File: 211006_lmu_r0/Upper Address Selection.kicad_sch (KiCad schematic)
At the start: 8 parts

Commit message: Updated some components to make sourcing easier
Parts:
- R103, R104, R105, R106, R107, R108, R109, R110: Manufacturer (none) -> -; Part Number (none) -> -
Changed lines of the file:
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@@
+      (effects (font (size 1.27 1.27)) hide)
+    )
+    (property "Part Number" "-" (id 4) (at 135.89 92.71 0)
+      (effects (font (size 1.27 1.27)) hide)
+    )
+    (property "Manufacturer" "-" (id 5) (at 135.89 92.71 0)
       (effects (font (size 1.27 1.27)) hide)
     )
@@
       (effects (font (size 1.27 1.27)) hide)
     )
+    (property "Part Number" "-" (id 4) (at 135.89 100.33 0)
+      (effects (font (size 1.27 1.27)) hide)
+    )
+    (property "Manufacturer" "-" (id 5) (at 135.89 100.33 0)
+      (effects (font (size 1.27 1.27)) hide)
+    )
     (pin "1")
     (pin "2")
@@
     )
     (property "Datasheet" "~" (id 3) (at 127 92.71 0)
+      (effects (font (size 1.27 1.27)) hide)
+    )
+    (property "Part Number" "-" (id 4) (at 127 92.71 0)
+      (effects (font (size 1.27 1.27)) hide)
+    )
+    (property "Manufacturer" "-" (id 5) (at 127 92.71 0)
       (effects (font (size 1.27 1.27)) hide)
     )
@@
       (effects (font (size 1.27 1.27)) hide)
     )
+    (property "Part Number" "-" (id 4) (at 127 100.33 0)
+      (effects (font (size 1.27 1.27)) hide)
+    )
+    (property "Manufacturer" "-" (id 5) (at 127 100.33 0)
+      (effects (font (size 1.27 1.27)) hide)
+    )
     (pin "1")
     (pin "2")
@@
     )
     (property "Datasheet" "~" (id 3) (at 143.51 92.71 0)
+      (effects (font (size 1.27 1.27)) hide)
+    )
+    (property "Part Number" "-" (id 4) (at 143.51 92.71 0)
+      (effects (font (size 1.27 1.27)) hide)
+    )
+    (property "Manufacturer" "-" (id 5) (at 143.51 92.71 0)
       (effects (font (size 1.27 1.27)) hide)
     )
@@
       (effects (font (size 1.27 1.27)) hide)
     )
+    (property "Part Number" "-" (id 4) (at 143.51 100.33 0)
+      (effects (font (size 1.27 1.27)) hide)
+    )
+    (property "Manufacturer" "-" (id 5) (at 143.51 100.33 0)
+      (effects (font (size 1.27 1.27)) hide)
+    )
     (pin "1")
     (pin "2")
@@
     )
     (property "Datasheet" "~" (id 3) (at 151.13 92.71 0)
+      (effects (font (size 1.27 1.27)) hide)
+    )
+    (property "Part Number" "-" (id 4) (at 151.13 92.71 0)
+      (effects (font (size 1.27 1.27)) hide)
+    )
+    (property "Manufacturer" "-" (id 5) (at 151.13 92.71 0)
       (effects (font (size 1.27 1.27)) hide)
     )
@@
       (effects (font (size 1.27 1.27)) hide)
     )
+    (property "Part Number" "-" (id 4) (at 151.13 100.33 0)
+      (effects (font (size 1.27 1.27)) hide)
+    )
+    (property "Manufacturer" "-" (id 5) (at 151.13 100.33 0)
+      (effects (font (size 1.27 1.27)) hide)
+    )

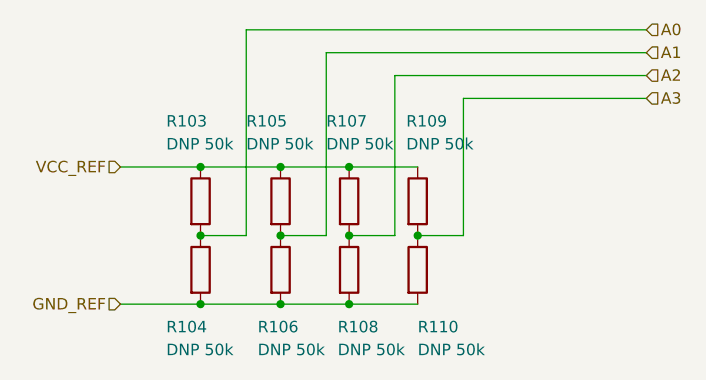
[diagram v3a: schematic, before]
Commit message: Lots of routing and placing, according to planned layout
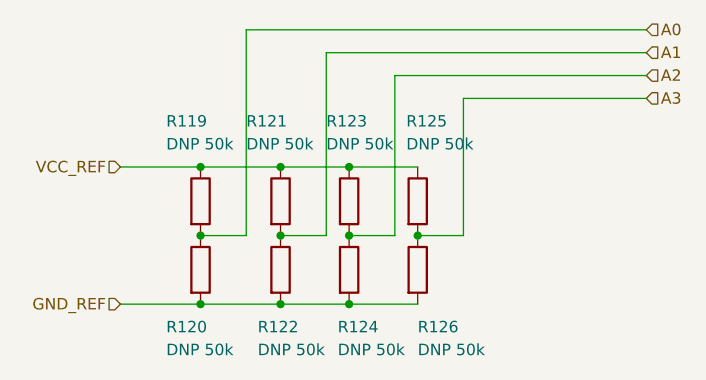
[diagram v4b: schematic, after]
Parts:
- renumbered R103 to R119, R104 to R120, R105 to R121, R106 to R122, R107 to R123, R108 to R124, R109 to R125, R110 to R126
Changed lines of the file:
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@@
   (symbol (lib_id "Device:R") (at 135.89 92.71 0)
     (in_bom yes) (on_board yes)
-    (property "Reference" "R105" (id 0) (at 132.08 83.82 0)
+    (property "Reference" "R121" (id 0) (at 132.08 83.82 0)
       (effects (font (size 1.27 1.27)) (justify left))
     )
@@
   (symbol (lib_id "Device:R") (at 135.89 100.33 0)
     (in_bom yes) (on_board yes)
-    (property "Reference" "R106" (id 0) (at 133.35 106.68 0)
+    (property "Reference" "R122" (id 0) (at 133.35 106.68 0)
       (effects (font (size 1.27 1.27)) (justify left))
     )
@@
   (symbol (lib_id "Device:R") (at 127 92.71 0)
     (in_bom yes) (on_board yes)
-    (property "Reference" "R103" (id 0) (at 123.19 83.82 0)
+    (property "Reference" "R119" (id 0) (at 123.19 83.82 0)
       (effects (font (size 1.27 1.27)) (justify left))
     )
@@
   (symbol (lib_id "Device:R") (at 127 100.33 0)
     (in_bom yes) (on_board yes)
-    (property "Reference" "R104" (id 0) (at 123.19 106.68 0)
+    (property "Reference" "R120" (id 0) (at 123.19 106.68 0)
       (effects (font (size 1.27 1.27)) (justify left))
     )
@@
   (symbol (lib_id "Device:R") (at 143.51 92.71 0)
     (in_bom yes) (on_board yes)
-    (property "Reference" "R107" (id 0) (at 140.97 83.82 0)
+    (property "Reference" "R123" (id 0) (at 140.97 83.82 0)
       (effects (font (size 1.27 1.27)) (justify left))
     )
@@
   (symbol (lib_id "Device:R") (at 143.51 100.33 0)
     (in_bom yes) (on_board yes)
-    (property "Reference" "R108" (id 0) (at 142.24 106.68 0)
+    (property "Reference" "R124" (id 0) (at 142.24 106.68 0)
       (effects (font (size 1.27 1.27)) (justify left))
     )
@@
   (symbol (lib_id "Device:R") (at 151.13 92.71 0)
     (in_bom yes) (on_board yes)
-    (property "Reference" "R109" (id 0) (at 149.86 83.82 0)
+    (property "Reference" "R125" (id 0) (at 149.86 83.82 0)
       (effects (font (size 1.27 1.27)) (justify left))
     )
@@
   (symbol (lib_id "Device:R") (at 151.13 100.33 0)
     (in_bom yes) (on_board yes)
-    (property "Reference" "R110" (id 0) (at 151.13 106.68 0)
+    (property "Reference" "R126" (id 0) (at 151.13 106.68 0)
       (effects (font (size 1.27 1.27)) (justify left))
     )

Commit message: trying out a quick thing, recover
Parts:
- renumbered R119 to R111, R120 to R112, R121 to R113, R122 to R114, R123 to R115, R124 to R116, R125 to R117, R126 to R118
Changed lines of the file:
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@@
   (symbol (lib_id "Device:R") (at 135.89 92.71 0)
     (in_bom yes) (on_board yes)
-    (property "Reference" "R121" (id 0) (at 132.08 83.82 0)
+    (property "Reference" "R113" (id 0) (at 132.08 83.82 0)
       (effects (font (size 1.27 1.27)) (justify left))
     )
@@
   (symbol (lib_id "Device:R") (at 135.89 100.33 0)
     (in_bom yes) (on_board yes)
-    (property "Reference" "R122" (id 0) (at 133.35 106.68 0)
+    (property "Reference" "R114" (id 0) (at 133.35 106.68 0)
       (effects (font (size 1.27 1.27)) (justify left))
     )
@@
   (symbol (lib_id "Device:R") (at 127 92.71 0)
     (in_bom yes) (on_board yes)
-    (property "Reference" "R119" (id 0) (at 123.19 83.82 0)
+    (property "Reference" "R111" (id 0) (at 123.19 83.82 0)
       (effects (font (size 1.27 1.27)) (justify left))
     )
@@
   (symbol (lib_id "Device:R") (at 127 100.33 0)
     (in_bom yes) (on_board yes)
-    (property "Reference" "R120" (id 0) (at 123.19 106.68 0)
+    (property "Reference" "R112" (id 0) (at 123.19 106.68 0)
       (effects (font (size 1.27 1.27)) (justify left))
     )
@@
   (symbol (lib_id "Device:R") (at 143.51 92.71 0)
     (in_bom yes) (on_board yes)
-    (property "Reference" "R123" (id 0) (at 140.97 83.82 0)
+    (property "Reference" "R115" (id 0) (at 140.97 83.82 0)
       (effects (font (size 1.27 1.27)) (justify left))
     )
@@
   (symbol (lib_id "Device:R") (at 143.51 100.33 0)
     (in_bom yes) (on_board yes)
-    (property "Reference" "R124" (id 0) (at 142.24 106.68 0)
+    (property "Reference" "R116" (id 0) (at 142.24 106.68 0)
       (effects (font (size 1.27 1.27)) (justify left))
     )
@@
   (symbol (lib_id "Device:R") (at 151.13 92.71 0)
     (in_bom yes) (on_board yes)
-    (property "Reference" "R125" (id 0) (at 149.86 83.82 0)
+    (property "Reference" "R117" (id 0) (at 149.86 83.82 0)
       (effects (font (size 1.27 1.27)) (justify left))
     )
@@
   (symbol (lib_id "Device:R") (at 151.13 100.33 0)
     (in_bom yes) (on_board yes)
-    (property "Reference" "R126" (id 0) (at 151.13 106.68 0)
+    (property "Reference" "R118" (id 0) (at 151.13 106.68 0)
       (effects (font (size 1.27 1.27)) (justify left))
     )

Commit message: routed ltc3811 accessories
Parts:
- renumbered R111 to R119, R112 to R120, R113 to R121, R114 to R122, R115 to R123, R116 to R124, R117 to R125, R118 to R126
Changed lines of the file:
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@@
   (symbol (lib_id "Device:R") (at 135.89 92.71 0)
     (in_bom yes) (on_board yes)
-    (property "Reference" "R113" (id 0) (at 132.08 83.82 0)
+    (property "Reference" "R121" (id 0) (at 132.08 83.82 0)
       (effects (font (size 1.27 1.27)) (justify left))
     )
@@
   (symbol (lib_id "Device:R") (at 135.89 100.33 0)
     (in_bom yes) (on_board yes)
-    (property "Reference" "R114" (id 0) (at 133.35 106.68 0)
+    (property "Reference" "R122" (id 0) (at 133.35 106.68 0)
       (effects (font (size 1.27 1.27)) (justify left))
     )
@@
   (symbol (lib_id "Device:R") (at 127 92.71 0)
     (in_bom yes) (on_board yes)
-    (property "Reference" "R111" (id 0) (at 123.19 83.82 0)
+    (property "Reference" "R119" (id 0) (at 123.19 83.82 0)
       (effects (font (size 1.27 1.27)) (justify left))
     )
@@
   (symbol (lib_id "Device:R") (at 127 100.33 0)
     (in_bom yes) (on_board yes)
-    (property "Reference" "R112" (id 0) (at 123.19 106.68 0)
+    (property "Reference" "R120" (id 0) (at 123.19 106.68 0)
       (effects (font (size 1.27 1.27)) (justify left))
     )
@@
   (symbol (lib_id "Device:R") (at 143.51 92.71 0)
     (in_bom yes) (on_board yes)
-    (property "Reference" "R115" (id 0) (at 140.97 83.82 0)
+    (property "Reference" "R123" (id 0) (at 140.97 83.82 0)
       (effects (font (size 1.27 1.27)) (justify left))
     )
@@
   (symbol (lib_id "Device:R") (at 143.51 100.33 0)
     (in_bom yes) (on_board yes)
-    (property "Reference" "R116" (id 0) (at 142.24 106.68 0)
+    (property "Reference" "R124" (id 0) (at 142.24 106.68 0)
       (effects (font (size 1.27 1.27)) (justify left))
     )
@@
   (symbol (lib_id "Device:R") (at 151.13 92.71 0)
     (in_bom yes) (on_board yes)
-    (property "Reference" "R117" (id 0) (at 149.86 83.82 0)
+    (property "Reference" "R125" (id 0) (at 149.86 83.82 0)
       (effects (font (size 1.27 1.27)) (justify left))
     )
@@
   (symbol (lib_id "Device:R") (at 151.13 100.33 0)
     (in_bom yes) (on_board yes)
-    (property "Reference" "R118" (id 0) (at 151.13 106.68 0)
+    (property "Reference" "R126" (id 0) (at 151.13 106.68 0)
       (effects (font (size 1.27 1.27)) (justify left))
     )

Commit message: going to bulk edit fields
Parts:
- R103: renamed from R119; value DNP 50k -> 50k DNP
- R104: renamed from R120; value DNP 50k -> 50k DNP
- R105: renamed from R121; value DNP 50k -> 50k DNP
- R106: renamed from R122; value DNP 50k -> 50k DNP
- R107: renamed from R123; value DNP 50k -> 50k DNP
- R108: renamed from R124; value DNP 50k -> 50k DNP
- R109: renamed from R125; value DNP 50k -> 50k DNP
- R110: renamed from R126; value DNP 50k -> 50k DNP
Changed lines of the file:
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@@
   (symbol (lib_id "Device:R") (at 135.89 92.71 0)
     (in_bom yes) (on_board yes)
-    (property "Reference" "R121" (id 0) (at 132.08 83.82 0)
+    (property "Reference" "R105" (id 0) (at 132.08 83.82 0)
       (effects (font (size 1.27 1.27)) (justify left))
     )
-    (property "Value" "DNP 50k" (id 1) (at 132.08 86.36 0)
+    (property "Value" "50k DNP" (id 1) (at 132.08 86.36 0)
       (effects (font (size 1.27 1.27)) (justify left))
     )
@@
   (symbol (lib_id "Device:R") (at 135.89 100.33 0)
     (in_bom yes) (on_board yes)
-    (property "Reference" "R122" (id 0) (at 133.35 106.68 0)
+    (property "Reference" "R106" (id 0) (at 133.35 106.68 0)
       (effects (font (size 1.27 1.27)) (justify left))
     )
-    (property "Value" "DNP 50k" (id 1) (at 133.35 109.22 0)
+    (property "Value" "50k DNP" (id 1) (at 133.35 109.22 0)
       (effects (font (size 1.27 1.27)) (justify left))
     )
@@
   (symbol (lib_id "Device:R") (at 127 92.71 0)
     (in_bom yes) (on_board yes)
-    (property "Reference" "R119" (id 0) (at 123.19 83.82 0)
+    (property "Reference" "R103" (id 0) (at 123.19 83.82 0)
       (effects (font (size 1.27 1.27)) (justify left))
     )
-    (property "Value" "DNP 50k" (id 1) (at 123.19 86.36 0)
+    (property "Value" "50k DNP" (id 1) (at 123.19 86.36 0)
       (effects (font (size 1.27 1.27)) (justify left))
     )
@@
   (symbol (lib_id "Device:R") (at 127 100.33 0)
     (in_bom yes) (on_board yes)
-    (property "Reference" "R120" (id 0) (at 123.19 106.68 0)
+    (property "Reference" "R104" (id 0) (at 123.19 106.68 0)
       (effects (font (size 1.27 1.27)) (justify left))
     )
-    (property "Value" "DNP 50k" (id 1) (at 123.19 109.22 0)
+    (property "Value" "50k DNP" (id 1) (at 123.19 109.22 0)
       (effects (font (size 1.27 1.27)) (justify left))
     )
@@
   (symbol (lib_id "Device:R") (at 143.51 92.71 0)
     (in_bom yes) (on_board yes)
-    (property "Reference" "R123" (id 0) (at 140.97 83.82 0)
+    (property "Reference" "R107" (id 0) (at 140.97 83.82 0)
       (effects (font (size 1.27 1.27)) (justify left))
     )
-    (property "Value" "DNP 50k" (id 1) (at 140.97 86.36 0)
+    (property "Value" "50k DNP" (id 1) (at 140.97 86.36 0)
       (effects (font (size 1.27 1.27)) (justify left))
     )
@@
   (symbol (lib_id "Device:R") (at 143.51 100.33 0)
     (in_bom yes) (on_board yes)
-    (property "Reference" "R124" (id 0) (at 142.24 106.68 0)
+    (property "Reference" "R108" (id 0) (at 142.24 106.68 0)
       (effects (font (size 1.27 1.27)) (justify left))
     )
-    (property "Value" "DNP 50k" (id 1) (at 142.24 109.22 0)
+    (property "Value" "50k DNP" (id 1) (at 142.24 109.22 0)
       (effects (font (size 1.27 1.27)) (justify left))
     )
@@
   (symbol (lib_id "Device:R") (at 151.13 92.71 0)
     (in_bom yes) (on_board yes)
-    (property "Reference" "R125" (id 0) (at 149.86 83.82 0)
+    (property "Reference" "R109" (id 0) (at 149.86 83.82 0)
       (effects (font (size 1.27 1.27)) (justify left))
     )
-    (property "Value" "DNP 50k" (id 1) (at 149.86 86.36 0)
+    (property "Value" "50k DNP" (id 1) (at 149.86 86.36 0)
       (effects (font (size 1.27 1.27)) (justify left))
     )
@@
   (symbol (lib_id "Device:R") (at 151.13 100.33 0)
     (in_bom yes) (on_board yes)
-    (property "Reference" "R126" (id 0) (at 151.13 106.68 0)
+    (property "Reference" "R110" (id 0) (at 151.13 106.68 0)
       (effects (font (size 1.27 1.27)) (justify left))
     )
-    (property "Value" "DNP 50k" (id 1) (at 151.13 109.22 0)
+    (property "Value" "50k DNP" (id 1) (at 151.13 109.22 0)
       (effects (font (size 1.27 1.27)) (justify left))
     )

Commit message: started to export and fix things
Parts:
- renumbered R103 to R119, R104 to R120, R105 to R121, R106 to R122, R107 to R123, R108 to R124, R109 to R125, R110 to R126
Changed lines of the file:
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@@
   (symbol (lib_id "Device:R") (at 135.89 92.71 0)
     (in_bom yes) (on_board yes)
-    (property "Reference" "R105" (id 0) (at 132.08 83.82 0)
+    (property "Reference" "R121" (id 0) (at 132.08 83.82 0)
       (effects (font (size 1.27 1.27)) (justify left))
     )
@@
   (symbol (lib_id "Device:R") (at 135.89 100.33 0)
     (in_bom yes) (on_board yes)
-    (property "Reference" "R106" (id 0) (at 133.35 106.68 0)
+    (property "Reference" "R122" (id 0) (at 133.35 106.68 0)
       (effects (font (size 1.27 1.27)) (justify left))
     )
@@
   (symbol (lib_id "Device:R") (at 127 92.71 0)
     (in_bom yes) (on_board yes)
-    (property "Reference" "R103" (id 0) (at 123.19 83.82 0)
+    (property "Reference" "R119" (id 0) (at 123.19 83.82 0)
       (effects (font (size 1.27 1.27)) (justify left))
     )
@@
   (symbol (lib_id "Device:R") (at 127 100.33 0)
     (in_bom yes) (on_board yes)
-    (property "Reference" "R104" (id 0) (at 123.19 106.68 0)
+    (property "Reference" "R120" (id 0) (at 123.19 106.68 0)
       (effects (font (size 1.27 1.27)) (justify left))
     )
@@
   (symbol (lib_id "Device:R") (at 143.51 92.71 0)
     (in_bom yes) (on_board yes)
-    (property "Reference" "R107" (id 0) (at 140.97 83.82 0)
+    (property "Reference" "R123" (id 0) (at 140.97 83.82 0)
       (effects (font (size 1.27 1.27)) (justify left))
     )
@@
   (symbol (lib_id "Device:R") (at 143.51 100.33 0)
     (in_bom yes) (on_board yes)
-    (property "Reference" "R108" (id 0) (at 142.24 106.68 0)
+    (property "Reference" "R124" (id 0) (at 142.24 106.68 0)
       (effects (font (size 1.27 1.27)) (justify left))
     )
@@
   (symbol (lib_id "Device:R") (at 151.13 92.71 0)
     (in_bom yes) (on_board yes)
-    (property "Reference" "R109" (id 0) (at 149.86 83.82 0)
+    (property "Reference" "R125" (id 0) (at 149.86 83.82 0)
       (effects (font (size 1.27 1.27)) (justify left))
     )
@@
   (symbol (lib_id "Device:R") (at 151.13 100.33 0)
     (in_bom yes) (on_board yes)
-    (property "Reference" "R110" (id 0) (at 151.13 106.68 0)
+    (property "Reference" "R126" (id 0) (at 151.13 106.68 0)
       (effects (font (size 1.27 1.27)) (justify left))
     )
